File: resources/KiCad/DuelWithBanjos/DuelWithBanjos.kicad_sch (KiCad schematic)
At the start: 21 parts, among them J4 01x03_Socket, J5 01x03_Pin, J6 01x03_Pin, J7 01x03_Socket

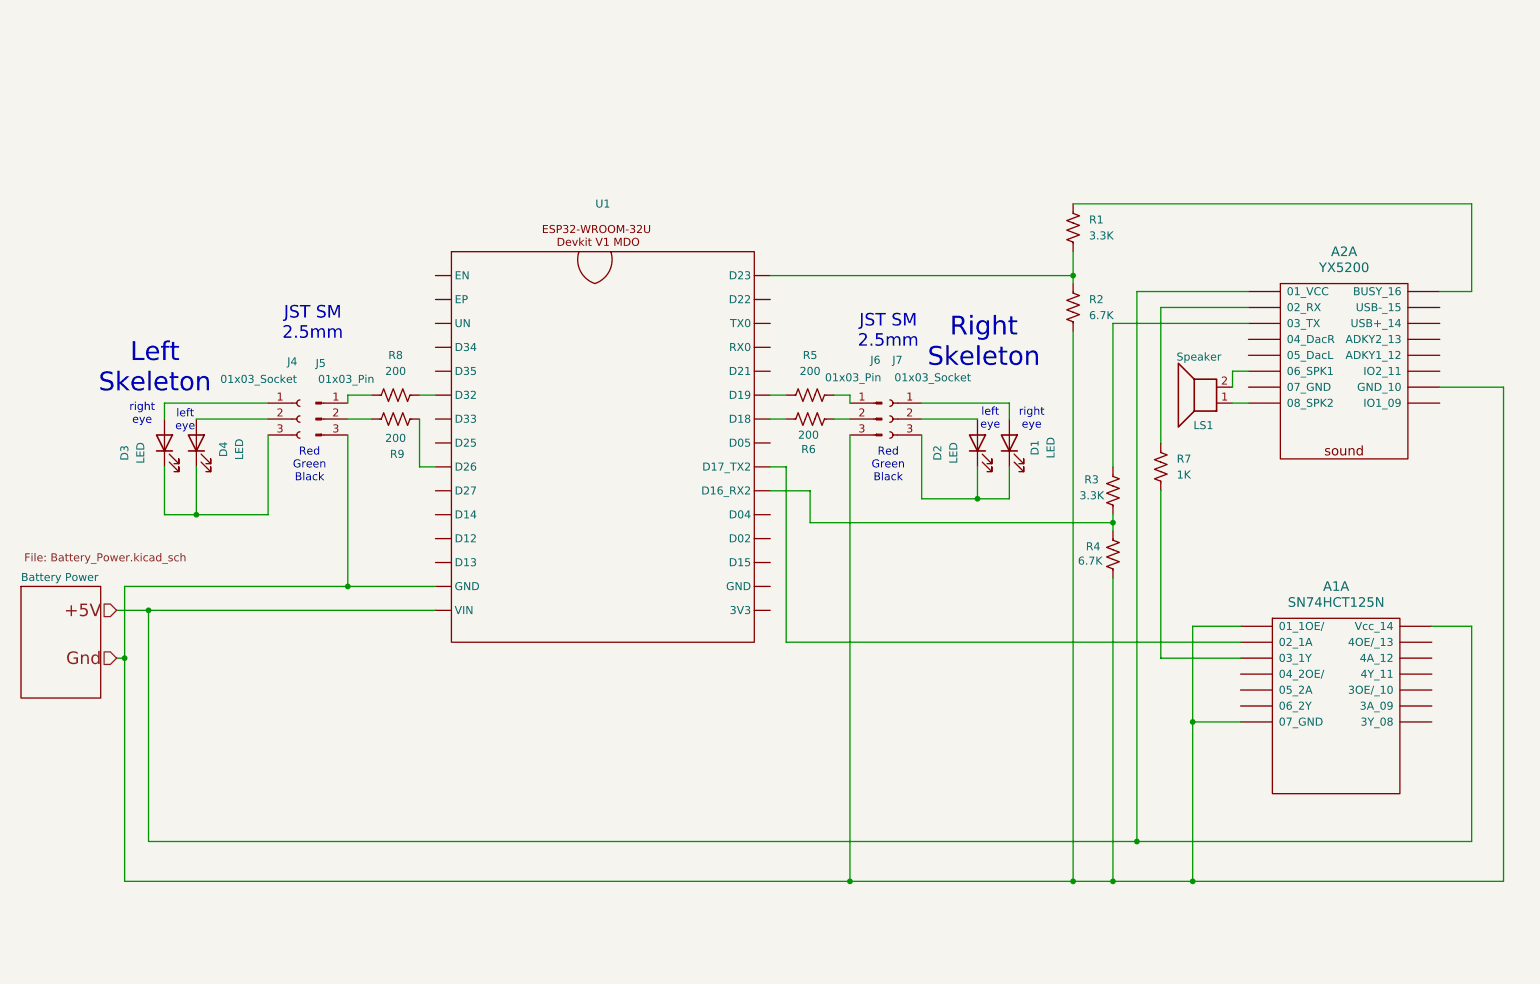
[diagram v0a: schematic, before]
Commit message: DS3502_digi_pot does not have enough current capacity on wiper
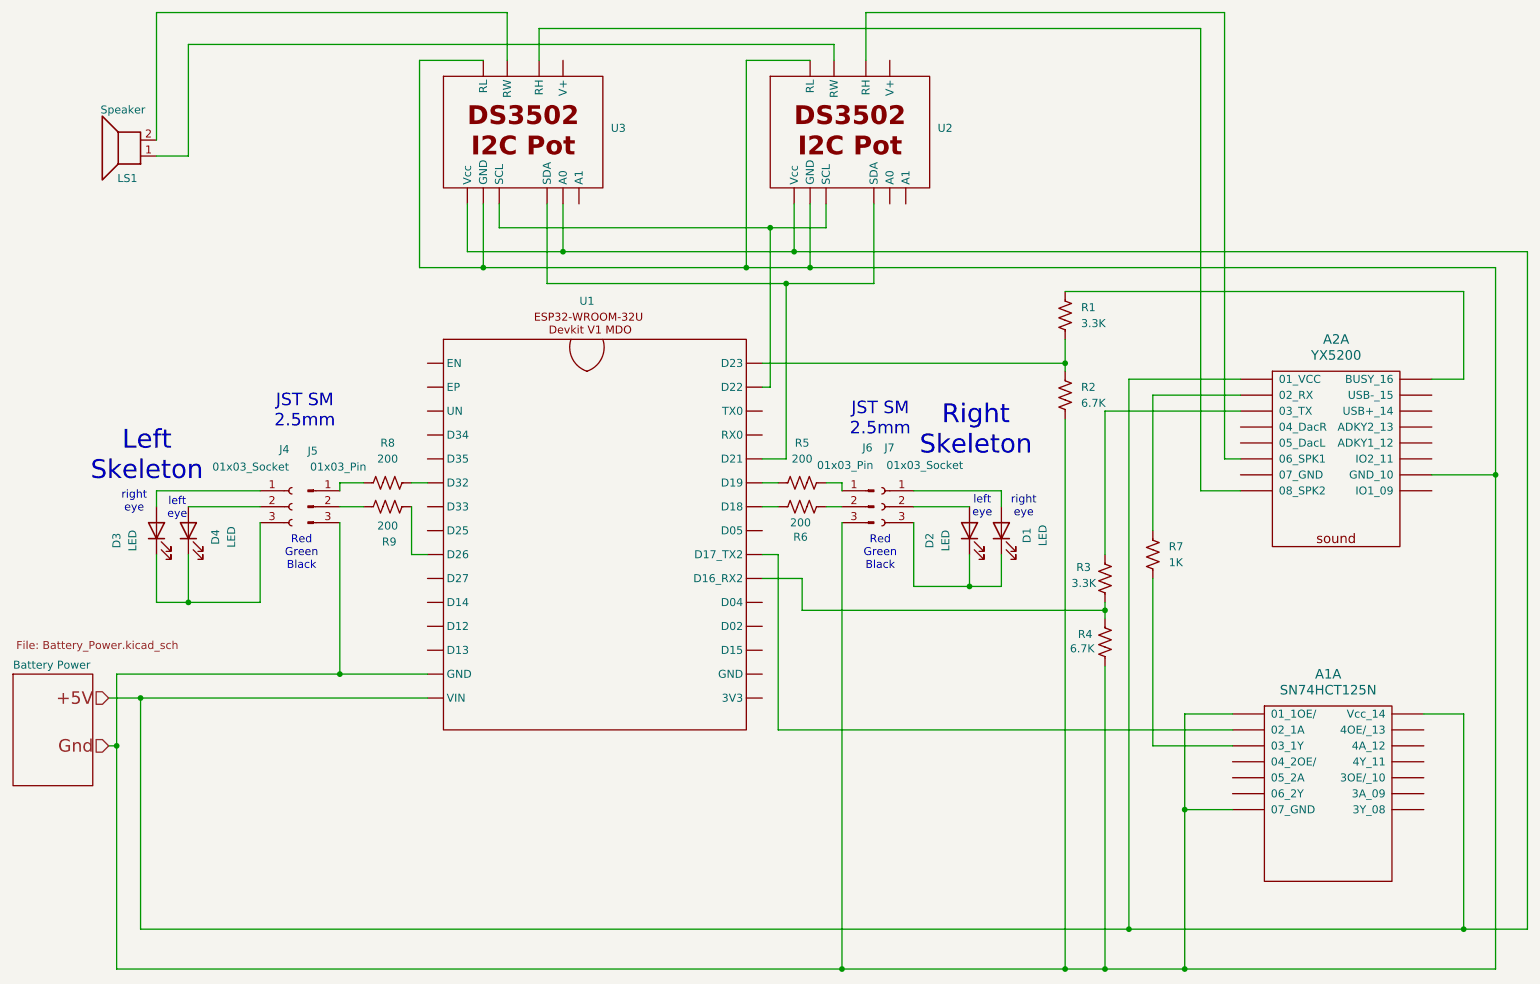
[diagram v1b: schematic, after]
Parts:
- added U2, U3: ~, symbol mdoLibrary:AF_DS5302_DigiPot
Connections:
- net +5V : now also U2. (A1), U3. (A1)
- net Gnd : now also U2. (A1), U3. (A1)
- net at LS1.1: now also U2. (A1); no longer A2.~ (IO1_09)
- net at LS1.2: now also U3. (A1); no longer A2.~ (IO1_09)
- new net: U1. (3V3), U2. (A1), U3. (A1) (x2)
- new net: A2.~ (IO1_09), U3. (A1)
- new net: A1.~ (3Y_08), U1. (3V3)
- new net: A2.~ (IO1_09), U2. (A1)
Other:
- moved on the sheet: A1A, A2A, D1, D2, D3, D4, J4, J5, J6, J7, LS1, R1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
